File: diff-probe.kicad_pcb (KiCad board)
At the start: 2 copper layers, 125 x 70 mm, 34 parts, among them J1 Conn_01x02, J2 Conn_Coaxial, J3 Conn_01x03, U1 LTC6228xS8, U2 LTC6228xS8, U3 LTC6228xS8

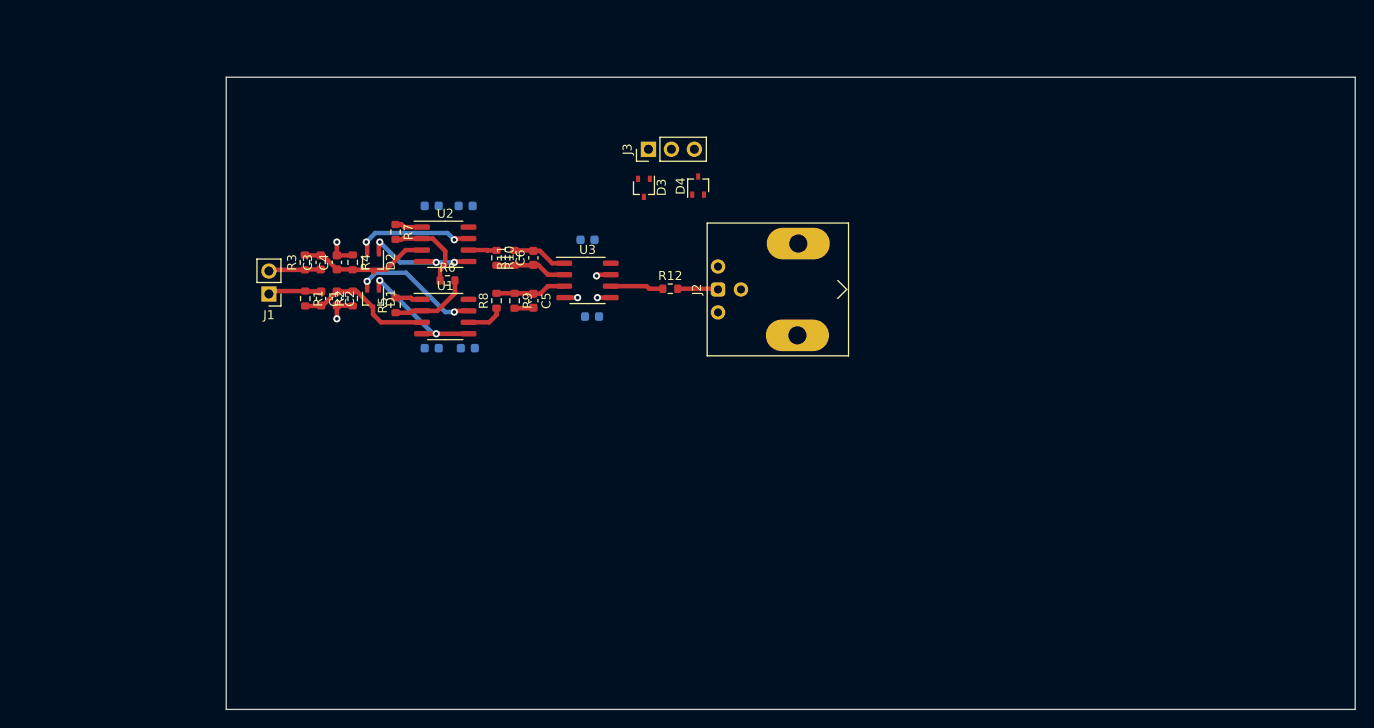
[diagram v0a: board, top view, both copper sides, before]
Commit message: Initial layout with SOIC op amp
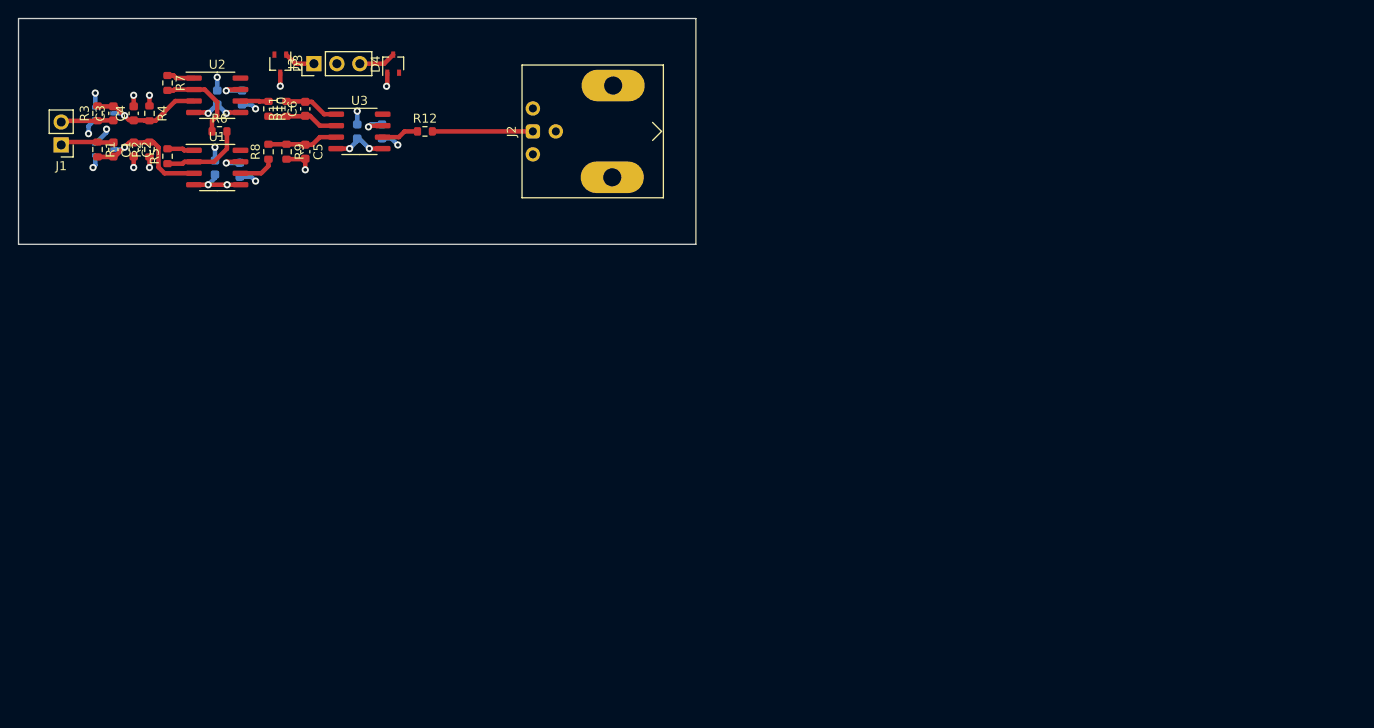
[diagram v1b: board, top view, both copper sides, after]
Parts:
- D1, D2: moved to B.Cu
- moved D3 42.5 mm to (59.0, 42.5)
- moved J3 38.2 mm to (62.7, 42.5)
- moved D4 36.4 mm to (71.5, 42.5)
- moved D1 34.0 mm to (39.5, 52.0), turned to 0 degrees
- moved D2 34.0 mm to (39.5, 48.0), turned to 0 degrees
- moved R12 32.3 mm to (75.0, 50.0)
- moved C10 32.1 mm to (54.5, 54.2), turned to -90 degrees
- moved C11 31.2 mm to (51.8, 54.0), turned to -90 degrees
- moved C30 31.0 mm to (70.2, 50.0), turned to -90 degrees
- moved C5 30.2 mm to (61.8, 52.2)
- moved C6 30.2 mm to (61.8, 47.5)
- moved R10 30.2 mm to (57.7, 47.5)
- moved R11 30.2 mm to (59.7, 47.5)
- moved R5 30.2 mm to (46.5, 52.8)
- moved R6 30.2 mm to (52.2, 50.0)
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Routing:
- net VSS: track 31.6 -> 76.0 mm, vias 7 -> 9
- net VDD: track 29.5 -> 66.1 mm, vias 5 -> 6
- net GND: track 8.59 -> 18.4 mm, vias 2 -> 11
- net /OUT: track 4.49 -> 11.2 mm
- net Net-(D4-Pad3): track 0.00 -> 4.11 mm
- net Net-(D3-Pad1): track 0.00 -> 3.49 mm
- net /DIFF: track 5.88 -> 4.11 mm
- net /ATTEN_NEG: track 14.6 -> 13.5 mm, vias 0 -> 1
- net /ATTEN_POS: track 15.5 -> 15.3 mm, vias 0 -> 1
- added copper zone on In1.Cu, net GND
- added copper zone on In2.Cu, net GND
- added copper zone on In2.Cu, net VDD
- added copper zone on In2.Cu, net VSS
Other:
- board size 125 x 70 mm -> 75 x 25 mm
- copper layers 2 -> 4

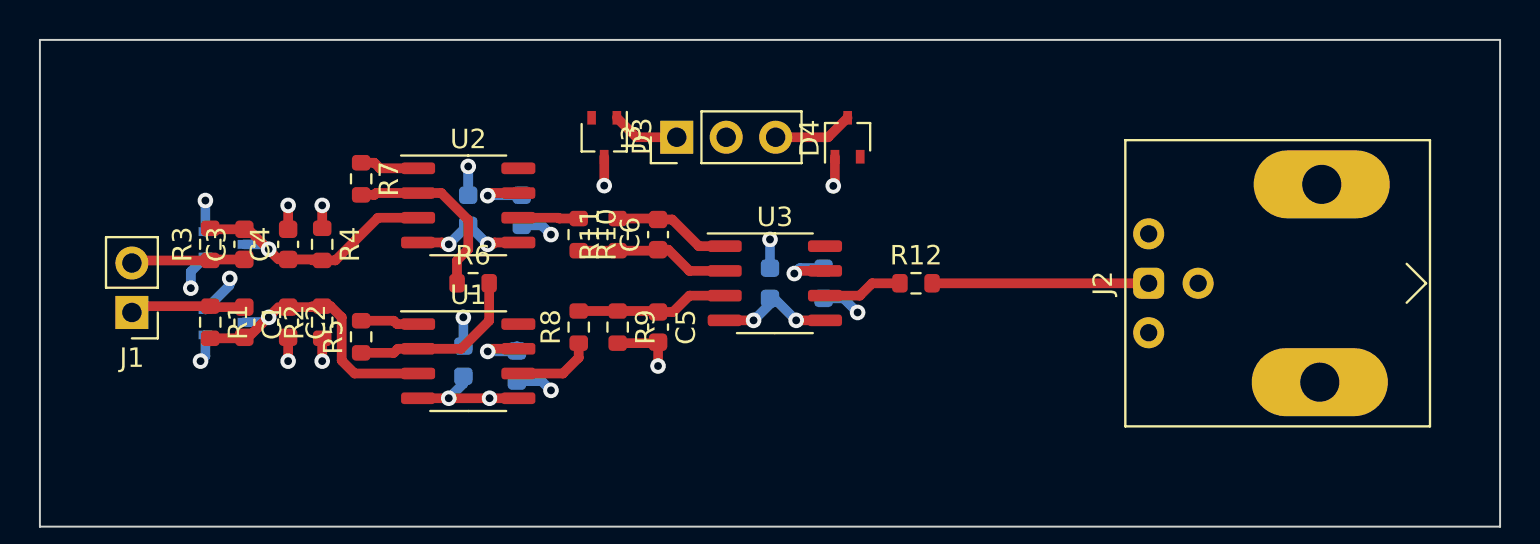
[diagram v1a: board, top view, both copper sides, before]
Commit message: Initial layout with SOT-23 op amp
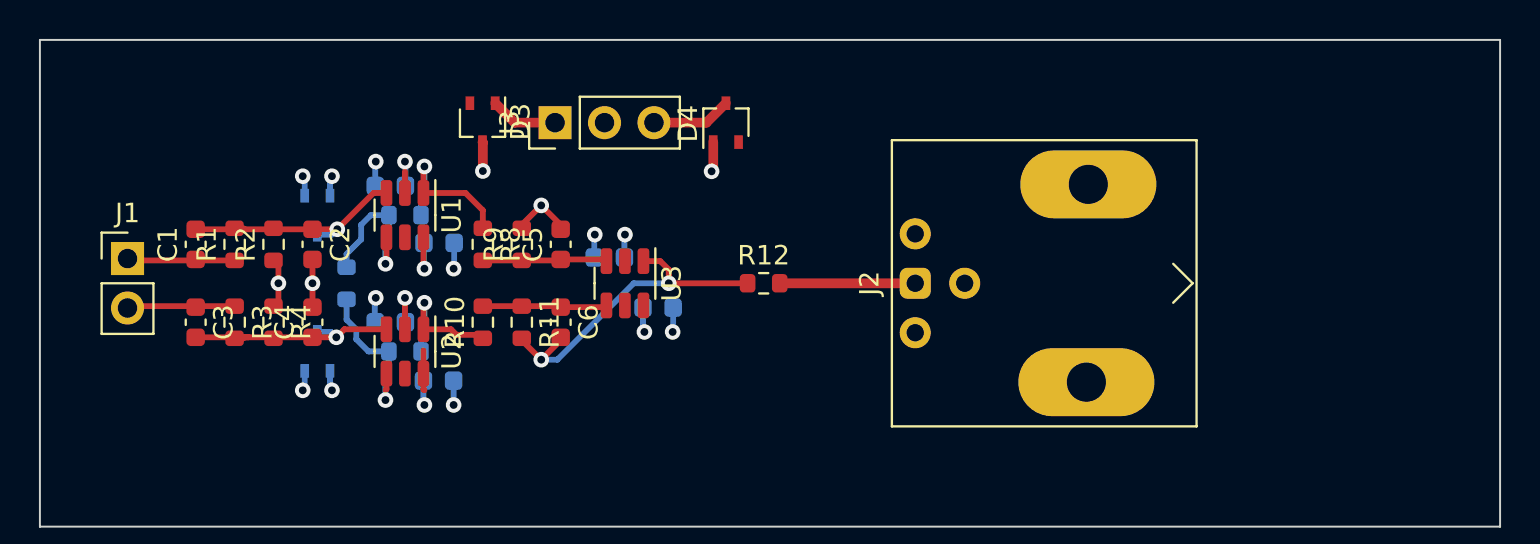
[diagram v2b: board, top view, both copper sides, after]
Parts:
- R5, R6, R7: moved to B.Cu
- U1, U2, U3: value LTC6228xS8 -> LTC6228xS6; footprint Package_SO:SO-8_3.9x4.9mm_P1.27mm -> Package_TO_SOT_SMD:TSOT-23-6
- moved J2 12.0 mm to (75.0, 50.0)
- moved R7 9.15 mm to (48.8, 53.5), turned to 180 degrees
- moved C30 8.59 mm to (61.8, 51.2), turned to 0 degrees
- moved C31 8.36 mm to (59.2, 48.7), turned to 0 degrees
- moved U1 8.17 mm to (48.8, 46.5), turned to -90 degrees
- moved U2 8.17 mm to (48.8, 53.5), turned to -90 degrees
- moved R12 7.83 mm to (67.2, 50.0)
- moved U3 7.70 mm to (60.0, 50.0), turned to -90 degrees
- moved D1 7.27 mm to (44.2, 46.5), turned to -90 degrees
- moved D2 7.27 mm to (44.2, 53.5), turned to 90 degrees
- moved C6 6.73 mm to (56.8, 52.0), turned to -90 degrees
- moved R10 6.67 mm to (52.8, 52.0), turned to 90 degrees
- moved R11 6.67 mm to (54.8, 52.0), turned to -90 degrees
- moved R5 6.64 mm to (48.8, 46.5), turned to 0 degrees
- moved C5 6.56 mm to (56.8, 48.0), turned to 90 degrees
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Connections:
- C6 pad 2: Net-(U3-Pad1) -> /DIFF
- R11 pad 2: Net-(U3-Pad1) -> /DIFF
- R5 pad 2: Net-(R5-Pad2) -> /BUF_POS
- R7 pad 1: Net-(R7-Pad1) -> /BUF_NEG
- U1 pad 1: Net-(R5-Pad2) -> /BUF_POS
- U1 pad 2: /FB_POS -> VSS
- U1 pad 4: VSS -> /FB_POS
- U1 pad 5: VSS -> unconnected-(U1-Pad5)
- U1 pad 6: /BUF_POS -> VDD
- U2 pad 1: Net-(R7-Pad1) -> /BUF_NEG
- U2 pad 2: /FB_NEG -> VSS
- U2 pad 4: VSS -> /FB_NEG
- U2 pad 5: VSS -> unconnected-(U2-Pad5)
- U2 pad 6: /BUF_NEG -> VDD
- U3 pad 1: Net-(U3-Pad1) -> /DIFF
- U3 pad 2: /DIFF_NEG -> VSS
- U3 pad 4: VSS -> /DIFF_NEG
- U3 pad 5: VSS -> unconnected-(U3-Pad5)
- U3 pad 6: /DIFF -> VDD
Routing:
- net VSS: track 76.0 -> 58.3 mm, vias 9 -> 6
- net /DIFF: track 4.11 -> 17.7 mm, vias 0 -> 2
- net Net-(U3-Pad1): track 6.09 -> 0.00 mm
- net VDD: track 66.1 -> 61.4 mm
- net /BUF_POS: track 4.19 -> 8.30 mm, vias 0 -> 1
- net /BUF_NEG: track 3.12 -> 7.12 mm, vias 0 -> 1
- net /OUT: track 11.2 -> 7.31 mm
- net /ATTEN_POS: track 15.3 -> 11.8 mm
- net Net-(R7-Pad1): track 3.04 -> 0.00 mm
- net Net-(R5-Pad2): track 3.00 -> 0.00 mm
- net /ATTEN_NEG: track 13.5 -> 11.4 mm
- net GND: track 18.4 -> 16.4 mm, vias 11 -> 9
- net /DIFF_NEG: track 7.97 -> 6.41 mm
- net /FB_NEG: track 9.60 -> 8.15 mm, vias 0 -> 1
- net /DIFF_POS: track 7.87 -> 6.57 mm
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- removed copper zone on In2.Cu, net VDD
- removed copper zone on In2.Cu, net VSS

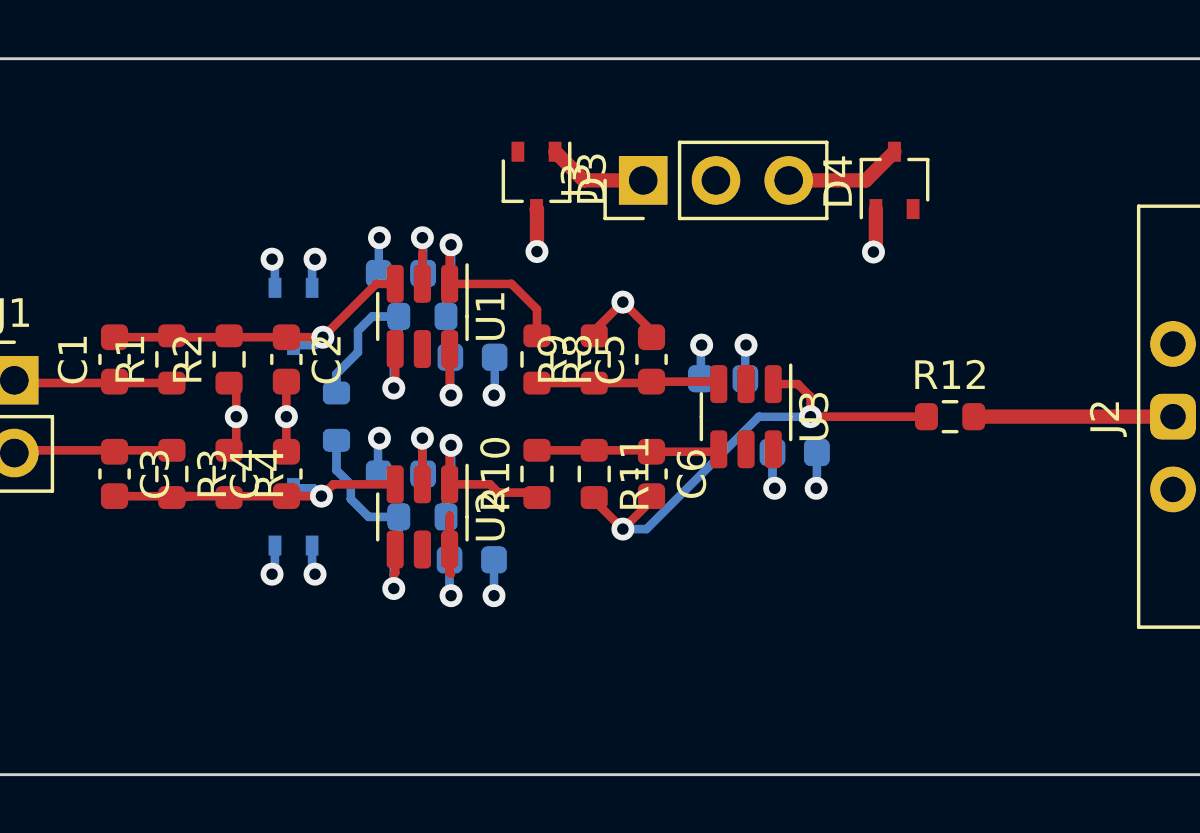
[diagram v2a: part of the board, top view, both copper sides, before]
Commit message: Start of alternate SOT layout
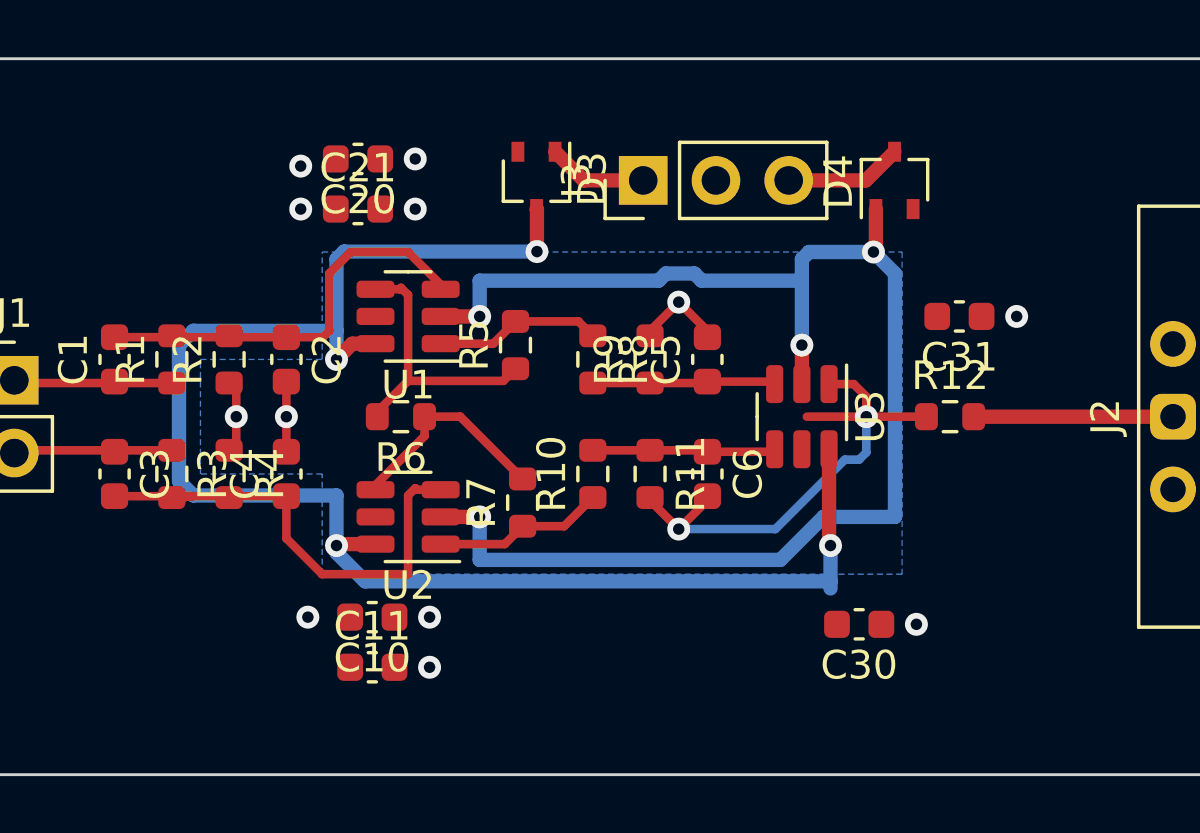
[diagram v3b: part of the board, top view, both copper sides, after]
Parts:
- removed D1, D2: BAT54SW, Package_TO_SOT_SMD:SOT-323_SC-70
- C10, C11, C20, C21, C30, C31, R5, R6, R7: moved to F.Cu
- moved C31 8.53 mm to (67.5, 46.5), turned to 180 degrees
- moved C20 8.00 mm to (46.5, 41.0), turned to 180 degrees
- moved C11 6.82 mm to (47.0, 58.8)
- moved C30 6.41 mm to (64.0, 57.2), turned to 180 degrees
- moved C10 4.01 mm to (47.0, 57.0), turned to 180 degrees
- moved R7 3.54 mm to (52.2, 53.0), turned to 90 degrees
- moved R5 3.40 mm to (52.0, 47.5), turned to 90 degrees
- moved C21 2.70 mm to (46.5, 42.8)
- moved R6 2.25 mm to (48.0, 50.0), turned to 180 degrees
- moved C5 1.95 mm to (58.7, 48.0)
- moved C6 1.95 mm to (58.7, 52.0)
- moved R10 1.95 mm to (54.7, 52.0)
- moved R11 1.95 mm to (56.7, 52.0)
- moved R8 1.95 mm to (54.7, 48.0)
- moved R9 1.95 mm to (56.7, 48.0)
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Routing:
- net GND: track 16.4 -> 8.10 mm, vias 9 -> 8
- net VSS: track 58.3 -> 50.2 mm, vias 6 -> 5
- net VDD: track 61.4 -> 55.9 mm, vias 6 -> 5
- net /ATTEN_NEG: track 11.4 -> 16.6 mm, vias 1 -> 0
- net /ATTEN_POS: track 11.8 -> 14.5 mm
- net /BUF_POS: track 8.30 -> 5.95 mm
- net /FB_POS: track 8.07 -> 9.88 mm, vias 1 -> 0
- net /BUF_NEG: track 7.12 -> 5.99 mm, vias 1 -> 0
- net /DIFF: track 17.7 -> 18.4 mm
- net /FB_NEG: track 8.15 -> 7.59 mm, vias 1 -> 0
- added copper zone on B.Cu, net GND
